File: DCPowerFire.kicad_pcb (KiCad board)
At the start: 4 copper layers, 51.7 x 7.9 mm, 50 parts, among them J1 Coil+/SafetySwitch, J10 NTC2_SIG, J11 NTC2_GND, J12 SafetySwitch, J2 BAT-, J3 USB_B_Micro, J4 NTC1_SIG, J5 NTC1_GND, J6 Conn_02x03_Odd_Even, J7 BAT+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

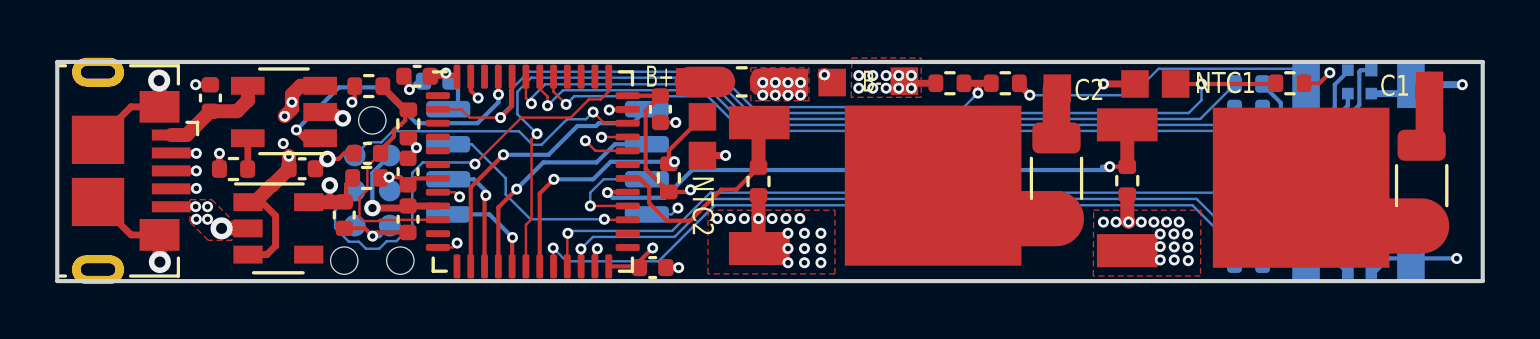
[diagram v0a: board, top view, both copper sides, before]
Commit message: increase via sizes to 0.2/0.45mm
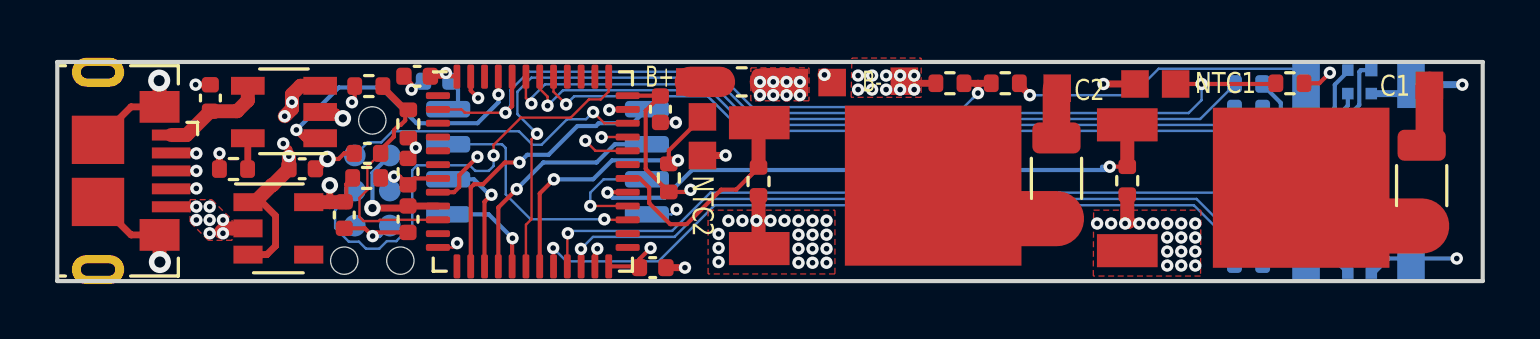
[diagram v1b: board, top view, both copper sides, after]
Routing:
- net GND: track 29.9 -> 31.4 mm, vias 65 -> 72
- net RST: track 7.98 -> 8.62 mm
- net SCK: track 15.9 -> 16.6 mm
- net +BATT: track 31.0 -> 31.6 mm

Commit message: minor fixes noticed during first assembly
resistor values, LED RGB mapping
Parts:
- C1, C3, C4: value 1µF -> 1u
- D1, D6: value LED_RGBA -> LED_BGRA
- F1: value Fuse -> 5A Fuse
- J1: value Coil+/SafetySwitch -> Coil+/LidSwitch
- J12: value SafetySwitch -> LidSwitch
- J3: value USB_B_Micro -> USB3076-30-A
- Q1, Q2: value IRF540N -> IRLR6225
- R1, R10, R2, R9: value R -> 82
- R11, R4: value R -> 270
- R12: value R -> 2k2
- R13, R14: value R -> 1M
- R15: value R -> 100
- R16, R17, R18, R20: value R -> 4k7
- R3, R5: value 27 ? -> 2 ?
- R6, R7: value R -> ?
- U4: value W25Q32JVSS -> GD25Q127CS
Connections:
- R1 pad 2: R_1 -> B_1
- R11 pad 2: B_2 -> R_2
- R4 pad 2: B_1 -> R_1
- R9 pad 2: R_2 -> B_2
- U3 pad 20: R_2 -> B_2
- U3 pad 21: B_2 -> R_2
- U3 pad 41: B_1 -> R_1
- U3 pad 42: R_1 -> B_1
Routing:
- net R_2: track 27.7 -> 26.5 mm
- net B_2: track 26.5 -> 27.7 mm
- net R_1: track 27.1 -> 26.1 mm
- net B_1: track 26.1 -> 27.1 mm
